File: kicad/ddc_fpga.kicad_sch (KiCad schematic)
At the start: 10 parts, among them U13 ICE40UP5K-SG48ITR

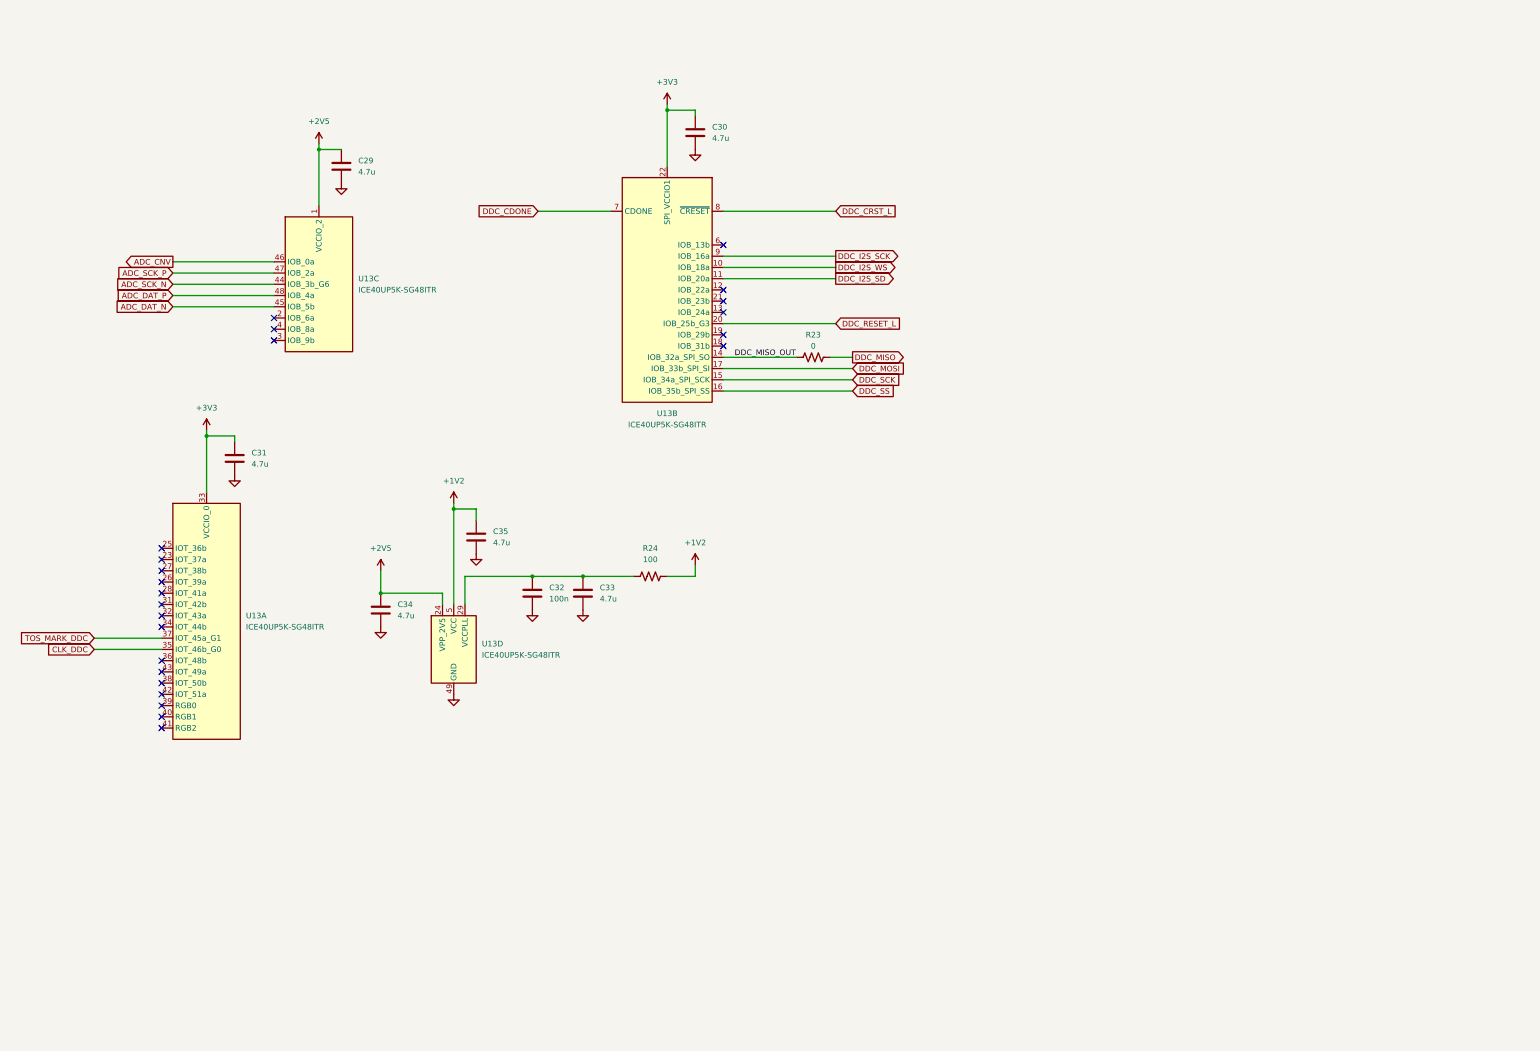
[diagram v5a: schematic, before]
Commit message: add triton t20, finish power connections
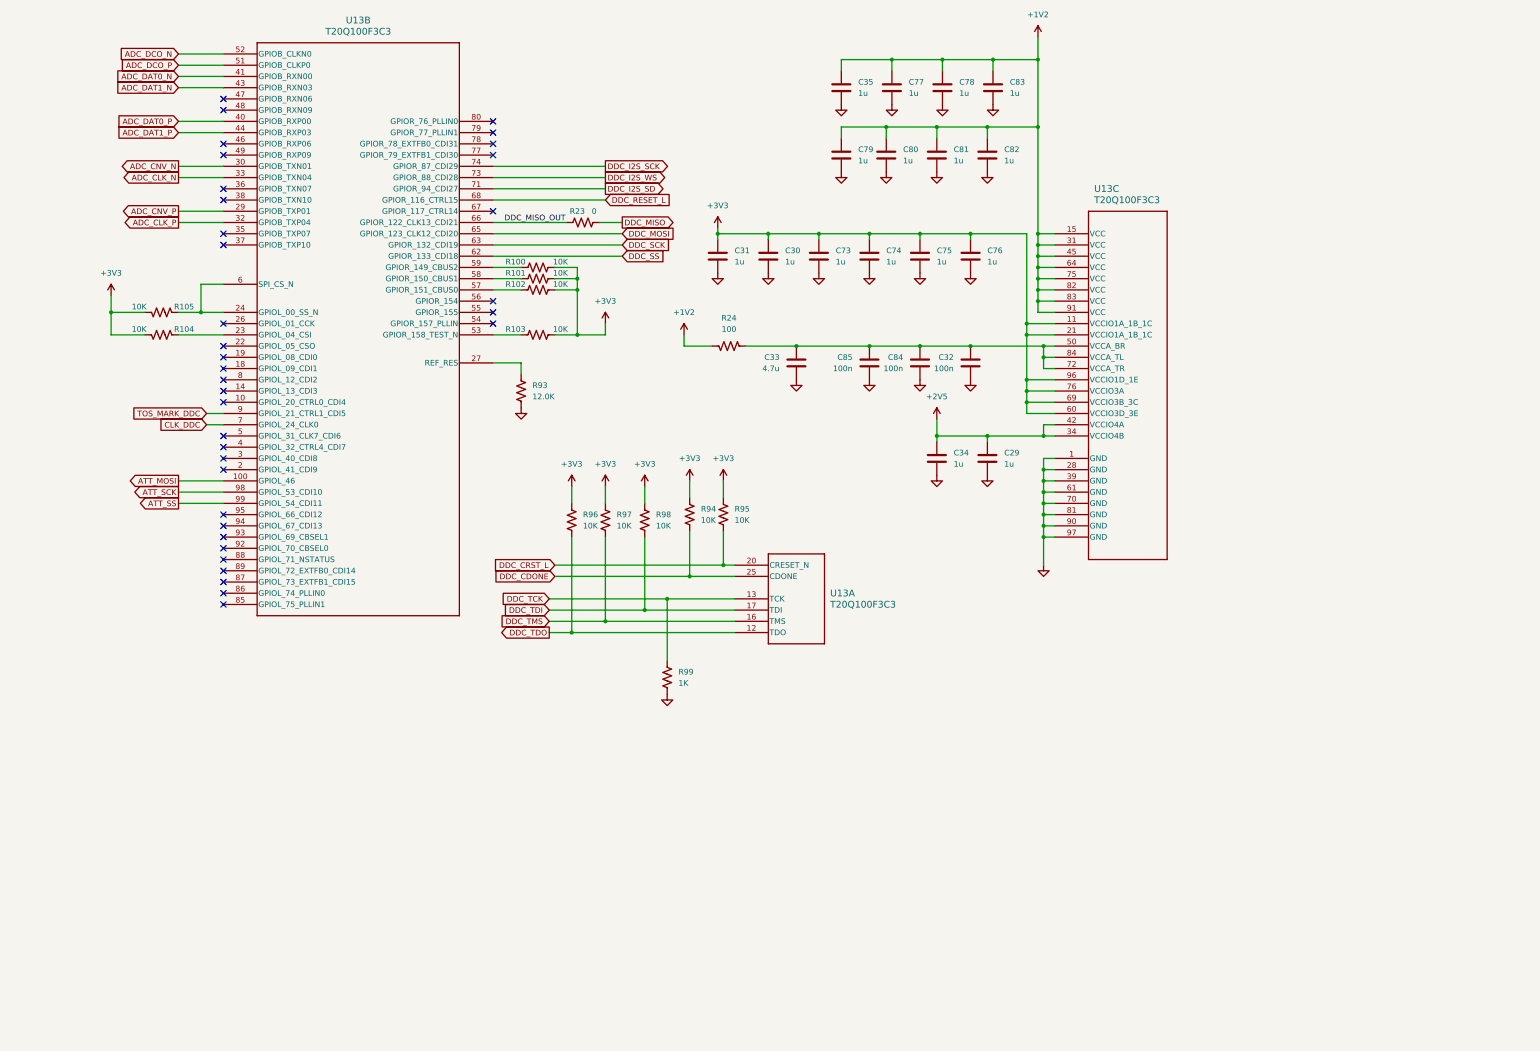
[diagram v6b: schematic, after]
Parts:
- removed U13: ICE40UP5K-SG48ITR, Package_DFN_QFN:QFN-48-1EP_7x7mm_P0.5mm_EP5.1x5.1mm, symbol FPGA_Lattice:ICE40UP5K-SG48ITR
- added C73, C74, C75, C76, C77, C78, C79, C80, C81, C82, C83: 1u, symbol Device:C
- added C84, C85: 100n, symbol Device:C
- added R100, R101, R102, R103, R104, R105, R94, R95, R96, R97, R98: 10K, symbol Device:R_US
- added R93: 12.0K, symbol Device:R_US
- added R99: 1K, symbol Device:R_US
- added U13: T20Q100F3C3, bgelb_footprint:LQFP100_TRION_EFI, symbol bgelb_lib:T20Q100F3C3
- C29, C30, C31, C34, C35: value 4.7u -> 1u
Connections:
- net +1V2: now also C77.1, C78.1, C79.1, C80.1, C81.1, C82.1, C83.1, U13.15 (VCC), U13.31 (VCC), U13.45 (VCC), U13.64 (VCC), U13.75 (VCC), U13.82 (VCC), U13.83 (VCC), U13.91 (VCC)
- net +2V5: now also U13.34 (VCCIO4B), U13.42 (VCCIO4A)
- net +3V3: now also C73.1, C74.1, C75.1, C76.1, R100.2, R101.2, R102.2, R103.2, R104.2, R105.2, R94.1, R95.1, R96.1, R97.1, R98.1, U13.11 (VCCIO1A_1B_1C), U13.21 (VCCIO1A_1B_1C), U13.60 (VCCIO3D_3E), U13.69 (VCCIO3B_3C), U13.76 (VCCIO3A), U13.96 (VCCIO1D_1E)
- net CLK_DDC: now also U13.7 (GPIOL_24_CLK0)
- net DDC_CDONE: now also R94.2, U13.25 (CDONE)
- net DDC_CRST_L: now also R95.2, U13.20 (CRESET_N)
- net DDC_I2S_SCK: now also U13.74 (GPIOR_87_CDI29)
- net DDC_I2S_SD: now also U13.71 (GPIOR_94_CDI27)
- net DDC_I2S_WS: now also U13.73 (GPIOR_88_CDI28)
- net DDC_MISO_OUT: now also U13.66 (GPIOR_122_CLK13_CDI21)
- net DDC_MOSI: now also U13.65 (GPIOR_123_CLK12_CDI20)
- net DDC_RESET_L: now also U13.68 (GPIOR_116_CTRL15)
- net DDC_SCK: now also U13.63 (GPIOR_132_CDI19)
- net DDC_SS: now also U13.62 (GPIOR_133_CDI18)
- net GND: now also C73.2, C74.2, C75.2, C76.2, C77.2, C78.2, C79.2, C80.2, C81.2, C82.2, C83.2, C84.2, C85.2, R93.2, R99.2, U13.1 (GND), U13.28 (GND), U13.39 (GND), U13.61 (GND), U13.70 (GND), U13.81 (GND), U13.90 (GND), U13.97 (GND)
- net TOS_MARK_DDC: now also U13.9 (GPIOL_21_CTRL1_CDI5)
- net at C32.1, C33.1, R24.1: now also C84.1, C85.1, U13.50 (VCCA_BR), U13.72 (VCCA_TR), U13.84 (VCCA_TL)
- new net: R100.1, U13.59 (GPIOR_149_CBUS2)
- new net: R105.1, U13.24 (GPIOL_00_SS_N), U13.6 (SPI_CS_N)
- new net: R102.1, U13.57 (GPIOR_151_CBUS0)
- new net: R103.1, U13.53 (GPIOR_158_TEST_N)
- new net: R93.1, U13.27 (REF_RES)
- new net: R104.1, U13.23 (GPIOL_04_CSI)
- new net: R101.1, U13.58 (GPIOR_150_CBUS1)
- new net ADC_CLK_N: U13.33 (GPIOB_TXN04)
- new net ADC_CLK_P: U13.32 (GPIOB_TXP04)
- new net ADC_CNV_N: U13.30 (GPIOB_TXN01)
- new net ADC_CNV_P: U13.29 (GPIOB_TXP01)
- new net ADC_DAT0_N: U13.41 (GPIOB_RXN00)
- new net ADC_DAT0_P: U13.40 (GPIOB_RXP00)
- new net ADC_DAT1_N: U13.43 (GPIOB_RXN03)
- new net ADC_DAT1_P: U13.44 (GPIOB_RXP03)
- new net ADC_DCO_N: U13.52 (GPIOB_CLKN0)
- new net ADC_DCO_P: U13.51 (GPIOB_CLKP0)
- new net ATT_MOSI: U13.100 (GPIOL_46)
- new net ATT_SCK: U13.98 (GPIOL_53_CDI10)
- new net ATT_SS: U13.99 (GPIOL_54_CDI11)
- new net DDC_TCK: R99.1, U13.13 (TCK)
- new net DDC_TDI: R98.2, U13.17 (TDI)
- new net DDC_TDO: R96.2, U13.12 (TDO)
- new net DDC_TMS: R97.2, U13.16 (TMS)
- no-connect marks 24 -> 36
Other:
- moved on the sheet: C29, C30, C31, C32, C33, C34, R23, R24

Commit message: add lte radio and various fixes
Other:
- moved on the sheet: C29, C30, C31, C32, C33, C34, C35, C73, C74, C75, C76, C77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

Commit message: assign footprints
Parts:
- C29, C30, C31, C32, C33, C34, C35, C73, C74, C75, C76, C77, C78, C79, C80, C81, C82, C83, C84, C85: footprint (none) -> Capacitor_SMD:C_0603_1608Metric_Pad1.08x0.95mm_HandSolder
- R100, R101, R102, R103, R104, R105, R23, R24, R93, R94, R95, R96, R97, R98, R99: footprint (none) -> Resistor_SMD:R_0603_1608Metric_Pad0.98x0.95mm_HandSolder
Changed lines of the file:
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@@
       (effects (font (size 1.27 1.27)) (justify left))
     )
-    (property "Footprint" "" (at 197.866 246.634 90)
+    (property "Footprint" "Resistor_SMD:R_0603_1608Metric_Pad0.98x0.95mm_HandSolder" (at 197.866 246.634 90)
       (effects (font (size 1.27 1.27)) hide)
     )
@@
       (effects (font (size 1.27 1.27)))
     )
-    (property "Footprint" "" (at 160.274 92.964 90)
+    (property "Footprint" "Resistor_SMD:R_0603_1608Metric_Pad0.98x0.95mm_HandSolder" (at 160.274 92.964 90)
       (effects (font (size 1.27 1.27)) hide)
     )
@@
       (effects (font (size 1.27 1.27)))
     )
-    (property "Footprint" "" (at 170.434 82.804 90)
+    (property "Footprint" "Resistor_SMD:R_0603_1608Metric_Pad0.98x0.95mm_HandSolder" (at 170.434 82.804 90)
       (effects (font (size 1.27 1.27)) hide)
     )
@@
       (effects (font (size 1.27 1.27)) (justify left))
     )
-    (property "Footprint" "" (at 309.5752 139.7 0)
+    (property "Footprint" "Capacitor_SMD:C_0603_1608Metric_Pad1.08x0.95mm_HandSolder" (at 309.5752 139.7 0)
       (effects (font (size 1.27 1.27)) hide)
     )
@@
       (effects (font (size 1.27 1.27)))
     )
-    (property "Footprint" "" (at 74.676 103.124 90)
+    (property "Footprint" "Resistor_SMD:R_0603_1608Metric_Pad0.98x0.95mm_HandSolder" (at 74.676 103.124 90)
       (effects (font (size 1.27 1.27)) hide)
     )
@@
       (effects (font (size 1.27 1.27)) (justify left))
     )
-    (property "Footprint" "" (at 210.566 209.804 90)
+    (property "Footprint" "Resistor_SMD:R_0603_1608Metric_Pad0.98x0.95mm_HandSolder" (at 210.566 209.804 90)
       (effects (font (size 1.27 1.27)) hide)
     )
@@
       (effects (font (size 1.27 1.27)) (justify left))
     )
-    (property "Footprint" "" (at 294.3352 93.98 0)
+    (property "Footprint" "Capacitor_SMD:C_0603_1608Metric_Pad1.08x0.95mm_HandSolder" (at 294.3352 93.98 0)
       (effects (font (size 1.27 1.27)) hide)
     )
@@
       (effects (font (size 1.27 1.27)))
     )
-    (property "Footprint" "" (at 160.274 98.044 90)
+    (property "Footprint" "Resistor_SMD:R_0603_1608Metric_Pad0.98x0.95mm_HandSolder" (at 160.274 98.044 90)
       (effects (font (size 1.27 1.27)) hide)
     )
@@
       (effects (font (size 1.27 1.27)) (justify left))
     )
-    (property "Footprint" "" (at 305.7652 93.98 0)
+    (property "Footprint" "Capacitor_SMD:C_0603_1608Metric_Pad1.08x0.95mm_HandSolder" (at 305.7652 93.98 0)
       (effects (font (size 1.27 1.27)) hide)
     )
@@
       (effects (font (size 1.27 1.27)) (justify left))
     )
-    (property "Footprint" "" (at 292.4048 118.11 0)
+    (property "Footprint" "Capacitor_SMD:C_0603_1608Metric_Pad1.08x0.95mm_HandSolder" (at 292.4048 118.11 0)
       (effects (font (size 1.27 1.27)) hide)
     )
@@
       (effects (font (size 1.27 1.27)) (justify left))
     )
-    (property "Footprint" "" (at 309.5752 71.12 0)
+    (property "Footprint" "Capacitor_SMD:C_0603_1608Metric_Pad1.08x0.95mm_HandSolder" (at 309.5752 71.12 0)
       (effects (font (size 1.27 1.27)) hide)
     )
@@
       (effects (font (size 1.27 1.27)) (justify left))
     )
-    (property "Footprint" "" (at 282.9052 93.98 0)
+    (property "Footprint" "Capacitor_SMD:C_0603_1608Metric_Pad1.08x0.95mm_HandSolder" (at 282.9052 93.98 0)
       (effects (font (size 1.27 1.27)) hide)
     )
@@
       (effects (font (size 1.27 1.27)))
     )
-    (property "Footprint" "" (at 160.274 108.204 90)
+    (property "Footprint" "Resistor_SMD:R_0603_1608Metric_Pad0.98x0.95mm_HandSolder" (at 160.274 108.204 90)
       (effects (font (size 1.27 1.27)) hide)
     )
@@
       (effects (font (size 1.27 1.27)) (justify left))
     )
-    (property "Footprint" "" (at 271.4752 93.98 0)
+    (property "Footprint" "Capacitor_SMD:C_0603_1608Metric_Pad1.08x0.95mm_HandSolder" (at 271.4752 93.98 0)
       (effects (font (size 1.27 1.27)) hide)
     )
@@
       (effects (font (size 1.27 1.27)) (justify left))
     )
-    (property "Footprint" "" (at 321.0052 139.7 0)
+    (property "Footprint" "Capacitor_SMD:C_0603_1608Metric_Pad1.08x0.95mm_HandSolder" (at 321.0052 139.7 0)
       (effects (font (size 1.27 1.27)) hide)
     )
@@
       (effects (font (size 1.27 1.27)) (justify left))
     )
-    (property "Footprint" "" (at 321.0052 71.12 0)
+    (property "Footprint" "Capacitor_SMD:C_0603_1608Metric_Pad1.08x0.95mm_HandSolder" (at 321.0052 71.12 0)
       (effects (font (size 1.27 1.27)) hide)
     )
@@
       (effects (font (size 1.27 1.27)) (justify left))
     )
-    (property "Footprint" "" (at 183.896 211.074 90)
+    (property "Footprint" "Resistor_SMD:R_0603_1608Metric_Pad0.98x0.95mm_HandSolder" (at 183.896 211.074 90)
       (effects (font (size 1.27 1.27)) hide)
     )
@@
       (effects (font (size 1.27 1.27)) (justify left))
     )
-    (property "Footprint" "" (at 317.1952 93.98 0)
+    (property "Footprint" "Capacitor_SMD:C_0603_1608Metric_Pad1.08x0.95mm_HandSolder" (at 317.1952 93.98 0)
       (effects (font (size 1.27 1.27)) hide)
     )
@@
       (effects (font (size 1.27 1.27)))
     )
-    (property "Footprint" "" (at 261.366 109.474 90)
+    (property "Footprint" "Resistor_SMD:R_0603_1608Metric_Pad0.98x0.95mm_HandSolder" (at 261.366 109.474 90)
       (effects (font (size 1.27 1.27)) hide)
     )
@@
       (effects (font (size 1.27 1.27)) (justify left))
     )
-    (property "Footprint" "" (at 157.226 122.174 90)
+    (property "Footprint" "Resistor_SMD:R_0603_1608Metric_Pad0.98x0.95mm_HandSolder" (at 157.226 122.174 90)
       (effects (font (size 1.27 1.27)) hide)
     )
@@
       (effects (font (size 1.27 1.27)) (justify left))
     )
-    (property "Footprint" "" (at 322.2752 55.88 0)
+    (property "Footprint" "Capacitor_SMD:C_0603_1608Metric_Pad1.08x0.95mm_HandSolder" (at 322.2752 55.88 0)
       (effects (font (size 1.27 1.27)) hide)
     )
@@
       (effects (font (size 1.27 1.27)) (justify left))
     )
-    (property "Footprint" "" (at 202.946 209.804 90)
+    (property "Footprint" "Resistor_SMD:R_0603_1608Metric_Pad0.98x0.95mm_HandSolder" (at 202.946 209.804 90)
       (effects (font (size 1.27 1.27)) hide)
     )
@@
       (effects (font (size 1.27 1.27)) (justify left))
     )
-    (property "Footprint" "" (at 176.276 211.074 90)
+    (property "Footprint" "Resistor_SMD:R_0603_1608Metric_Pad0.98x0.95mm_HandSolder" (at 176.276 211.074 90)
       (effects (font (size 1.27 1.27)) hide)
     )
@@
       (effects (font (size 1.27 1.27)) (justify left))
     )
-    (property "Footprint" "" (at 298.1452 71.12 0)
+    (property "Footprint" "Capacitor_SMD:C_0603_1608Metric_Pad1.08x0.95mm_HandSolder" (at 298.1452 71.12 0)
       (effects (font (size 1.27 1.27)) hide)
     )
@@
       (effects (font (size 1.27 1.27)) (justify left))
     )
-    (property "Footprint" "" (at 299.4152 55.88 0)
+    (property "Footprint" "Capacitor_SMD:C_0603_1608Metric_Pad1.08x0.95mm_HandSolder" (at 299.4152 55.88 0)
       (effects (font (size 1.27 1.27)) hide)
     )
@@
       (effects (font (size 1.27 1.27)) (justify left))
     )
-    (property "Footprint" "" (at 310.8452 55.88 0)
+    (property "Footprint" "Capacitor_SMD:C_0603_1608Metric_Pad1.08x0.95mm_HandSolder" (at 310.8452 55.88 0)
       (effects (font (size 1.27 1.27)) hide)
     )
@@
       (effects (font (size 1.27 1.27)))
     )
-    (property "Footprint" "" (at 74.676 108.204 90)
+    (property "Footprint" "Resistor_SMD:R_0603_1608Metric_Pad0.98x0.95mm_HandSolder" (at 74.676 108.204 90)
       (effects (font (size 1.27 1.27)) hide)
     )
@@
       (effects (font (size 1.27 1.27)) (justify left))
     )
-    (property "Footprint" "" (at 287.9852 71.12 0)
+    (property "Footprint" "Capacitor_SMD:C_0603_1608Metric_Pad1.08x0.95mm_HandSolder" (at 287.9852 71.12 0)
       (effects (font (size 1.27 1.27)) hide)
     )
@@
       (effects (font (size 1.27 1.27)))
     )
-    (property "Footprint" "" (at 160.274 95.504 90)
+    (property "Footprint" "Resistor_SMD:R_0603_1608Metric_Pad0.98x0.95mm_HandSolder" (at 160.274 95.504 90)
       (effects (font (size 1.27 1.27)) hide)
     )
@@
       (effects (font (size 1.27 1.27)) (justify left))
     )
-    (property "Footprint" "" (at 260.0452 93.98 0)
+    (property "Footprint" "Capacitor_SMD:C_0603_1608Metric_Pad1.08x0.95mm_HandSolder" (at 260.0452 93.98 0)
       (effects (font (size 1.27 1.27)) hide)
     )
@@
       (effects (font (size 1.27 1.27)) (justify left))
     )
-    (property "Footprint" "" (at 303.8348 118.11 0)
+    (property "Footprint" "Capacitor_SMD:C_0603_1608Metric_Pad1.08x0.95mm_HandSolder" (at 303.8348 118.11 0)
       (effects (font (size 1.27 1.27)) hide)
     )
@@
       (effects (font (size 1.27 1.27)) (justify left))
     )
-    (property "Footprint" "" (at 287.9852 55.88 0)
+    (property "Footprint" "Capacitor_SMD:C_0603_1608Metric_Pad1.08x0.95mm_HandSolder" (at 287.9852 55.88 0)
       (effects (font (size 1.27 1.27)) hide)
     )
@@
       (effects (font (size 1.27 1.27)) (justify left))
     )
-    (property "Footprint" "" (at 275.8948 118.11 0)
+    (property "Footprint" "Capacitor_SMD:C_0603_1608Metric_Pad1.08x0.95mm_HandSolder" (at 275.8948 118.11 0)
       (effects (font (size 1.27 1.27)) hide)
     )
@@
       (effects (font (size 1.27 1.27)) (justify left))
     )
-    (property "Footprint" "" (at 315.2648 118.11 0)
+    (property "Footprint" "Capacitor_SMD:C_0603_1608Metric_Pad1.08x0.95mm_HandSolder" (at 315.2648 118.11 0)
       (effects (font (size 1.27 1.27)) hide)
     )
@@
       (effects (font (size 1.27 1.27)) (justify left))
     )
-    (property "Footprint" "" (at 192.786 211.074 90)
-      (effects (font (size 1.27 1.27)) hide)
-    )
+    (property "Footprint" "Resistor_SMD:R_0603_1608Metric_Pad0.98x0.95mm_HandSolder" (at 192.786 211.074 90)
+      (effects (font (size 1.27 1.27)) hide)
+    )
